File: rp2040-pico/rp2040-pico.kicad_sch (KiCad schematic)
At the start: 43 parts, among them J2 DIN41612_02x16_AB, J3 USB_C_Receptacle_USB2.0, J4 Micro_SD_Card_Det, Q7 DMG2305UX, Q8 DMG2305UX, SW3 SW_Push, U5 LM317_SOT-223

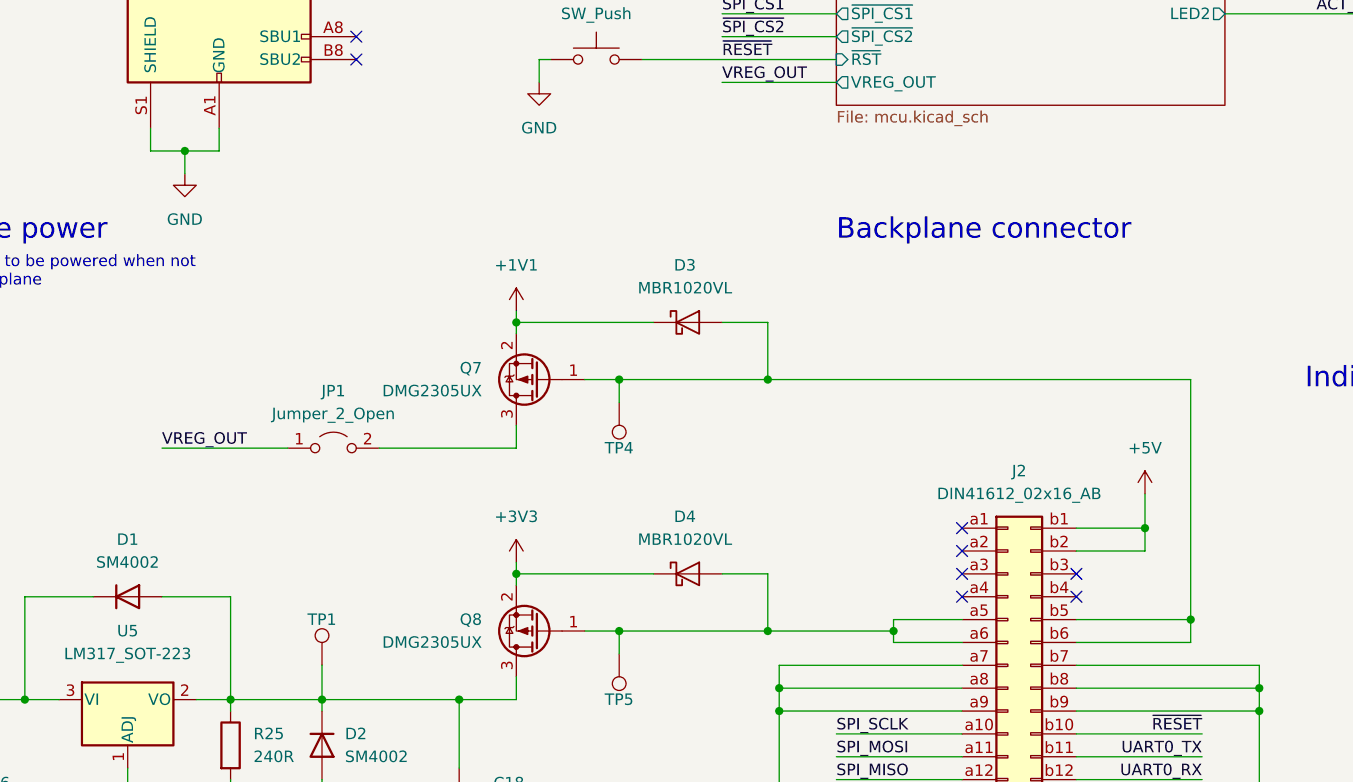
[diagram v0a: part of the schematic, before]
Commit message: Added rev 0.3 PCB + minor alterations to schematic
The PCB design work has been completed for rev 0.3 of the board. Some
minor changes to the schematic were made as issues were encountered
during board design. The most notable being the removal of unneccessary
test points and the addition of another P-channel mosfet to allow the 5V
rail to have two seperate power supplies.

Signed-off-by: Matthew Nickson <mnickson@sidingsmedia.com>
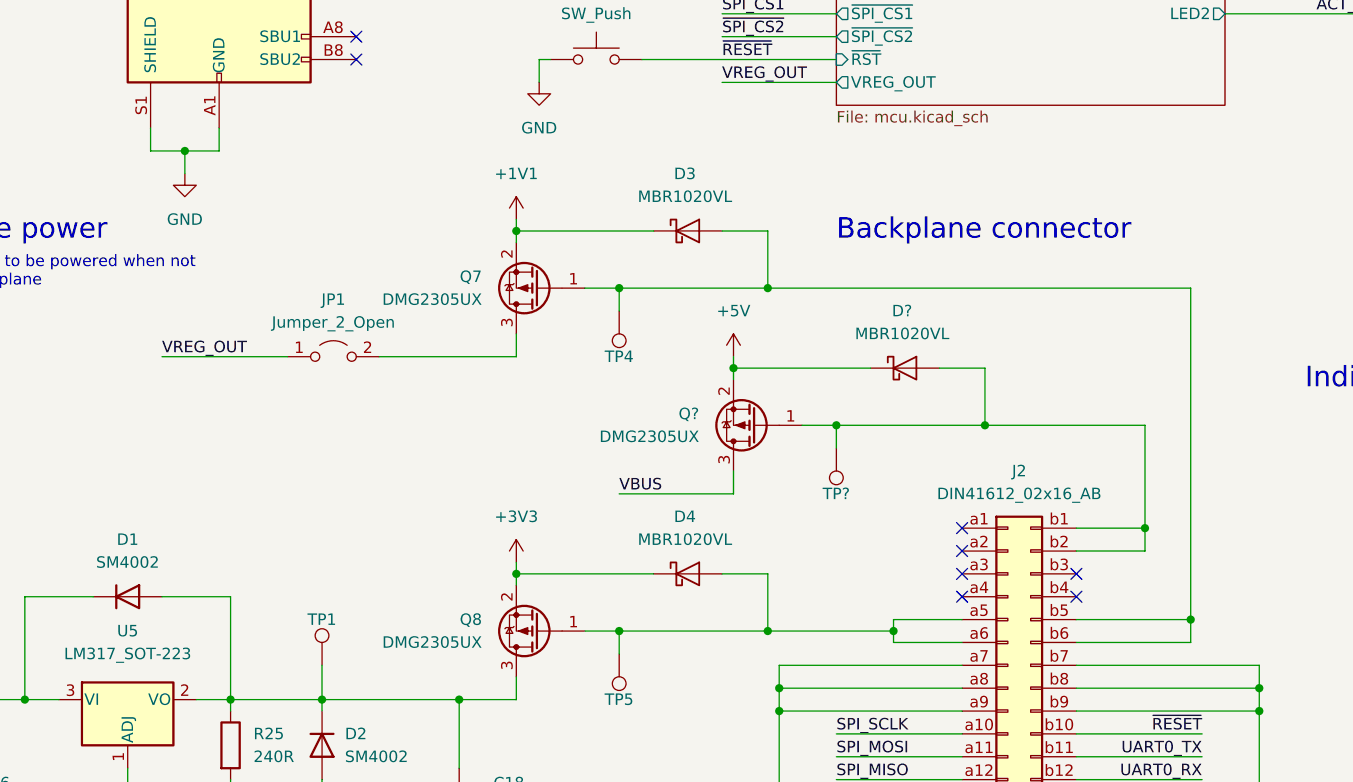
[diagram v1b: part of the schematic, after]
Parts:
- added D?: MBR1020VL, Diode_SMD:D_SOD-123F, symbol Diode:MBR1020VL
- added Q?: DMG2305UX, Package_TO_SOT_SMD:SOT-23, symbol Transistor_FET:DMG2301L
- added TP?: TestPoint, TestPoint:TestPoint_Pad_D1.0mm, symbol Connector:TestPoint
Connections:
- net +5V: now also D?.1 (K), Q?.2 (S); no longer J2.b1 (Pin_b1), J2.b2 (Pin_b2)
- net VBUS: now also Q?.3 (D)
- new net: D?.2 (A), J2.b1 (Pin_b1), J2.b2 (Pin_b2), Q?.1 (G), TP?.1
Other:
- moved on the sheet: D3, JP1, Q7, TP4

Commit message: Some minor changes and increment version number
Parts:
- gave numbers to parts that had none: 3
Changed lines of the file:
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@@
     (title "RP2040/Pico Main Control Board")
     (date "2022-11-20")
-    (rev "0.2")
+    (rev "0.3")
     (company "Sidings Media")
     (comment 1 "Licence: CERN-OHL-P-2.0 or any later version")
@@
   (symbol (lib_id "Transistor_FET:DMG2301L") (at 119.38 106.68 180) (unit 1)
     (in_bom yes) (on_board yes) (fields_autoplaced)
-    (property "Reference" "Q?" (id 0) (at 113.03 105.4099 0)
+    (property "Reference" "Q9" (id 0) (at 113.03 105.4099 0)
       (effects (font (size 1.27 1.27)) (justify left))
     )
@@
   (symbol (lib_id "power:+5V") (at 116.84 99.06 0) (unit 1)
     (in_bom yes) (on_board yes) (fields_autoplaced)
-    (property "Reference" "#PWR?" (id 0) (at 116.84 102.87 0)
+    (property "Reference" "#PWR025" (id 0) (at 116.84 102.87 0)
       (effects (font (size 1.27 1.27)) hide)
     )
@@
   (symbol (lib_id "Connector:TestPoint") (at 128.27 109.22 180) (unit 1)
     (in_bom yes) (on_board yes)
-    (property "Reference" "TP?" (id 0) (at 128.27 114.3 0))
+    (property "Reference" "TP18" (id 0) (at 128.27 114.3 0))
     (property "Value" "TestPoint" (id 1) (at 125.73 111.2521 0)
       (effects (font (size 1.27 1.27)) (justify left) hide)
@@
   (symbol (lib_id "Diode:MBR1020VL") (at 135.89 100.33 0) (unit 1)
     (in_bom yes) (on_board yes)
-    (property "Reference" "D?" (id 0) (at 135.5725 93.98 0))
+    (property "Reference" "D8" (id 0) (at 135.5725 93.98 0))
     (property "Value" "MBR1020VL" (id 1) (at 135.5725 96.52 0))
     (property "Footprint" "Diode_SMD:D_SOD-123F" (id 2) (at 135.89 104.775 0)
@@
       (reference "#PWR024") (unit 1) (value "GND") (footprint "")
     )
+    (path "/2bc78eb9-33bd-4ec0-93a8-07b0b899168b"
+      (reference "#PWR025") (unit 1) (value "+5V") (footprint "")
+    )
     (path "/3f1b00fa-7c07-4e68-8180-02fb9c5edd20"
       (reference "#PWR026") (unit 1) (value "GND") (footprint "")
@@
       (reference "#PWR049") (unit 1) (value "GND") (footprint "")
     )
-    (path "/2bc78eb9-33bd-4ec0-93a8-07b0b899168b"
-      (reference "#PWR?") (unit 1) (value "+5V") (footprint "")
-    )
     (path "/f88a2e30-f4d9-4749-be3c-3c9bf4f2c5b6/92d6a064-7bf0-4854-8f68-f21dccd2eea9"
       (reference "C1") (unit 1) (value "0.1uF") (footprint "Capacitor_SMD:C_0402_1005Metric_Pad0.74x0.62mm_HandSolder")
@@
     )
     (path "/bae283a3-77de-4f07-ad43-2f7d207a132a"
-      (reference "D?") (unit 1) (value "MBR1020VL") (footprint "Diode_SMD:D_SOD-123F")
+      (reference "D8") (unit 1) (value "MBR1020VL") (footprint "Diode_SMD:D_SOD-123F")
     )
     (path "/96aba777-9ddb-4238-bfd5-baee0b5d77c4"
@@
     )
     (path "/255897cd-577a-49cf-b1db-c7ca093d5552"
-      (reference "Q?") (unit 1) (value "DMG2305UX") (footprint "Package_TO_SOT_SMD:SOT-23")
+      (reference "Q9") (unit 1) (value "DMG2305UX") (footprint "Package_TO_SOT_SMD:SOT-23")
     )
     (path "/f88a2e30-f4d9-4749-be3c-3c9bf4f2c5b6/69070d9a-2a51-47d0-a485-e017644661b7"
@@
       (reference "TP17") (unit 1) (value "TestPoint") (footprint "TestPoint:TestPoint_Pad_D1.0mm")
     )
+    (path "/610b3310-ba0a-40e1-a2c2-d34ccd60552f"
+      (reference "TP18") (unit 1) (value "TestPoint") (footprint "TestPoint:TestPoint_Pad_D1.0mm")
+    )
     (path "/db5cc6ec-32e5-4752-8117-f03b0aab0c5f/c086ba49-5b0b-443f-9ba0-e2ff7fc8b22f"
       (reference "TP24") (unit 1) (value "TestPoint") (footprint "TestPoint:TestPoint_Pad_D1.0mm")
     )
-    (path "/610b3310-ba0a-40e1-a2c2-d34ccd60552f"
-      (reference "TP?") (unit 1) (value "TestPoint") (footprint "TestPoint:TestPoint_Pad_D1.0mm")
-    )
     (path "/f88a2e30-f4d9-4749-be3c-3c9bf4f2c5b6/3f3dfeae-ac77-4740-a1fc-64ca6140ff46"
